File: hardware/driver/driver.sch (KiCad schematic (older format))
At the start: 32 parts, among them J1 Conn_01x02, J2 Conn_01x02, J3 Conn_01x04, J4 Conn_01x04, J6 Conn_01x02, Q1 IRF9Z34NPBF, Q2 IRF9Z34NPBF, Q3 IRFZ24NPBF, Q4 IRFZ24NPBF, U1 TC4420CPA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

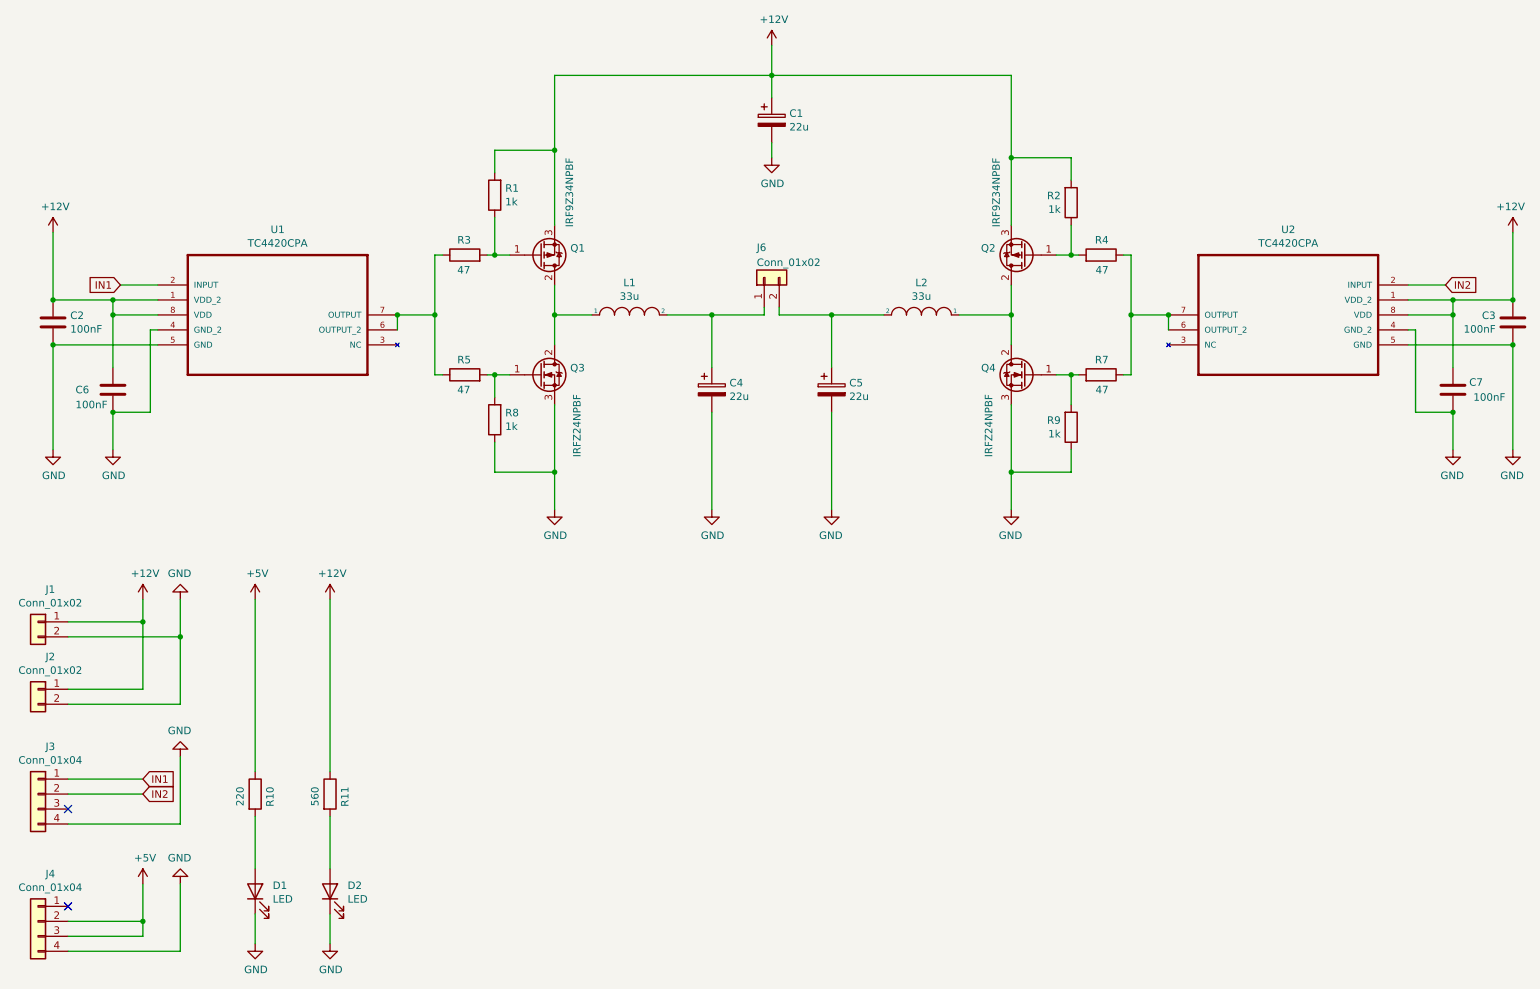
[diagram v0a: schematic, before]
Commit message: Update driver board
Driver board v0.1
Apart from removing temperature sensor connector, there are some minor changes:
- some tracks, such as 12V line near Q1 and Q3, were changed;
- 12V connectors are now moved to the "front panel" of the board.
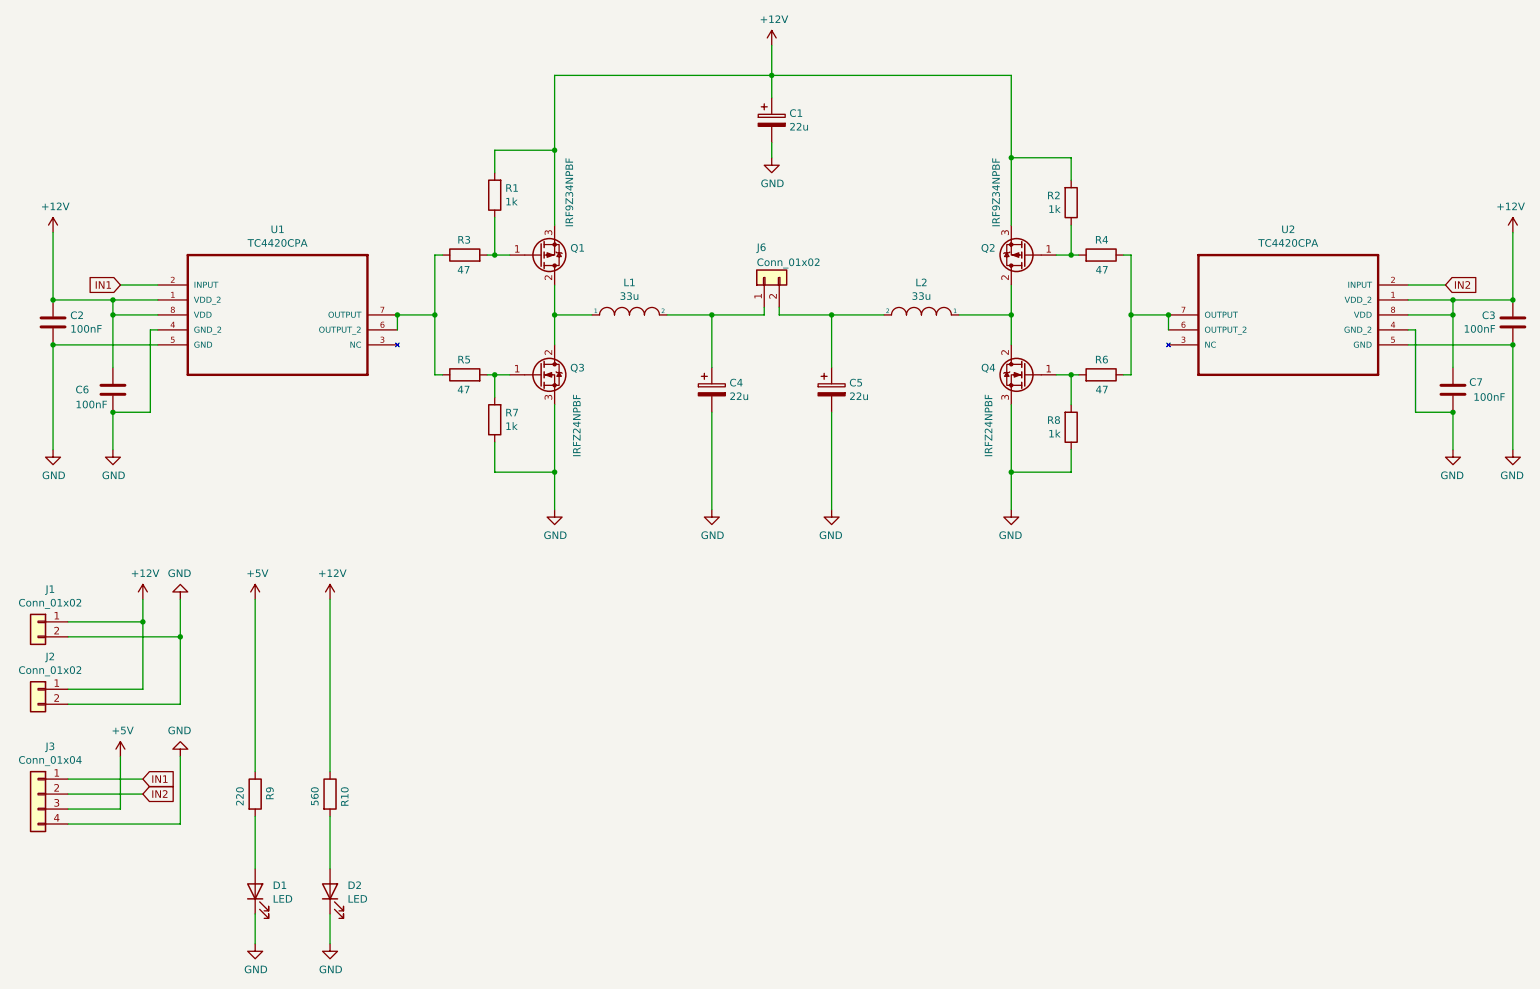
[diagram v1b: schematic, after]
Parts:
- removed J4: Conn_01x04, Connector_JST:JST_XH_B4B-XH-A_1x04_P2.50mm_Vertical, symbol Connector_Generic:Conn_01x04
- renumbered R11 to R10, R7 to R6, R8 to R7, R9 to R8, R10 to R9
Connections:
- net +5V: now also J3.3 (Pin_3)
- no-connect marks 2 -> 0
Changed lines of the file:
@@
 Wire Wire Line
 	950  6400 1450 6400
-$Comp
-L power:+5V #PWR08
-U 1 1 5F591312
-P 1450 7100
-F 0 "#PWR08" H 1450 6950 50  0001 C CNN
-F 1 "+5V" H 1465 7273 50  0000 C CNN
-F 2 "" H 1450 7100 50  0001 C CNN
-F 3 "" H 1450 7100 50  0001 C CNN
-	1    1450 7100
-	1    0    0    -1
-$EndComp
-$Comp
-L Connector_Generic:Conn_01x04 J4
-U 1 1 5F59DECB
-P 750 7350
-F 0 "J4" H 668 7667 50  0000 C CNN
-F 1 "Conn_01x04" H 668 7576 50  0000 C CNN
-F 2 "Connector_JST:JST_XH_B4B-XH-A_1x04_P2.50mm_Vertical" H 750 7350 50  0001 C CNN
-F 3 "~" H 750 7350 50  0001 C CNN
-	1    750  7350
-	-1   0    0    -1
-$EndComp
-$Comp
-L power:GND #PWR06
-U 1 1 5F59FAE5
-P 1700 7100
-F 0 "#PWR06" H 1700 6850 50  0001 C CNN
-F 1 "GND" H 1705 6927 50  0000 C CNN
-F 2 "" H 1700 7100 50  0001 C CNN
-F 3 "" H 1700 7100 50  0001 C CNN
-	1    1700 7100
-	-1   0    0    1
-$EndComp
 Text GLabel 1450 6500 2    50   Input ~ 0
 IN2
@@
 $EndComp
 $Comp
-L Device:R R8
+L Device:R R7
 U 1 1 5F64F957
 P 3800 4000
-F 0 "R8" H 3730 3954 50  0000 R CNN
+F 0 "R7" H 3730 3954 50  0000 R CNN
 F 1 "1k" H 3730 4045 50  0000 R CNN
 F 2 "Resistor_THT:R_Box_L13.0mm_W4.0mm_P9.00mm" V 3730 4000 50  0001 C CNN
@@
 Wire Wire Line
 	7650 2900 7550 2900
-$Comp
-L Device:R R9
-U 1 1 5F69B88C
-P 7650 4050
-F 0 "R9" H 7580 4004 50  0000 R CNN
-F 1 "1k" H 7580 4095 50  0000 R CNN
-F 2 "Resistor_THT:R_Box_L13.0mm_W4.0mm_P9.00mm" V 7580 4050 50  0001 C CNN
-F 3 "~" H 7650 4050 50  0001 C CNN
-	1    7650 4050
-	1    0    0    1
-$EndComp
 Wire Wire Line
 	7650 3900 7650 3700
@@
 	0    -1   -1   0
 $EndComp
-$Comp
-L Device:R R10
-U 1 1 5F6C1F80
-P 2200 6500
-F 0 "R10" V 2300 6550 50  0000 R CNN
-F 1 "220" V 2100 6550 50  0000 R CNN
-F 2 "Resistor_THT:R_Box_L13.0mm_W4.0mm_P9.00mm" V 2130 6500 50  0001 C CNN
-F 3 "~" H 2200 6500 50  0001 C CNN
-	1    2200 6500
-	1    0    0    -1
-$EndComp
 Wire Wire Line
 	2200 7000 2200 6650
@@
 $EndComp
 $Comp
-L Device:R R7
+L Device:R R6
 U 1 1 5F6331C6
 P 7850 3700
-F 0 "R7" V 7950 3750 50  0000 R CNN
+F 0 "R6" V 7950 3750 50  0000 R CNN
 F 1 "47" V 7750 3750 50  0000 R CNN
 F 2 "Resistor_THT:R_Box_L13.0mm_W4.0mm_P9.00mm" V 7780 3700 50  0001 C CNN
@@
 	0    -1   -1   0
 $EndComp
-$Comp
-L Device:R R11
-U 1 1 5F6D669A
-P 2700 6500
-F 0 "R11" V 2800 6550 50  0000 R CNN
-F 1 "560" V 2600 6550 50  0000 R CNN
-F 2 "Resistor_THT:R_Box_L13.0mm_W4.0mm_P9.00mm" V 2630 6500 50  0001 C CNN
-F 3 "~" H 2700 6500 50  0001 C CNN
-	1    2700 6500
-	1    0    0    -1
-$EndComp
 Wire Wire Line
 	2700 7000 2700 6650
@@
 Wire Wire Line
 	1700 6250 1700 6700
-NoConn ~ 950  6600
-Wire Wire Line
-	950  7450 1450 7450
-Wire Wire Line
-	1450 7100 1450 7350
-Wire Wire Line
-	1700 7100 1700 7550
-Wire Wire Line
-	950  7550 1700 7550
 Wire Wire Line
 	1700 5450 1700 5900
@@
 	-1   0    0    1
 $EndComp
-NoConn ~ 950  7250
-Wire Wire Line
-	950  7350 1450 7350
-Connection ~ 1450 7350
-Wire Wire Line
-	1450 7350 1450 7450
+$Comp
+L Device:R R10
+U 1 1 5F6D669A
+P 2700 6500
+F 0 "R10" V 2800 6550 50  0000 R CNN
+F 1 "560" V 2600 6550 50  0000 R CNN
+F 2 "Resistor_THT:R_Box_L13.0mm_W4.0mm_P9.00mm" V 2630 6500 50  0001 C CNN
+F 3 "~" H 2700 6500 50  0001 C CNN
+	1    2700 6500
+	1    0    0    -1
+$EndComp
+$Comp
+L Device:R R9
+U 1 1 5F6C1F80
+P 2200 6500
+F 0 "R9" V 2300 6550 50  0000 R CNN
+F 1 "220" V 2100 6550 50  0000 R CNN
+F 2 "Resistor_THT:R_Box_L13.0mm_W4.0mm_P9.00mm" V 2130 6500 50  0001 C CNN
+F 3 "~" H 2200 6500 50  0001 C CNN
+	1    2200 6500
+	1    0    0    -1
+$EndComp
+$Comp
+L Device:R R8
+U 1 1 5F69B88C
+P 7650 4050
+F 0 "R8" H 7580 4004 50  0000 R CNN
+F 1 "1k" H 7580 4095 50  0000 R CNN
+F 2 "Resistor_THT:R_Box_L13.0mm_W4.0mm_P9.00mm" V 7580 4050 50  0001 C CNN
+F 3 "~" H 7650 4050 50  0001 C CNN
+	1    7650 4050
+	1    0    0    1
+$EndComp
+$Comp
+L power:+5V #PWR?
+U 1 1 60A6900B
+P 1300 6250
+F 0 "#PWR?" H 1300 6100 50  0001 C CNN
+F 1 "+5V" H 1315 6423 50  0000 C CNN
+F 2 "" H 1300 6250 50  0001 C CNN
+F 3 "" H 1300 6250 50  0001 C CNN
+	1    1300 6250
+	1    0    0    -1
+$EndComp
+Wire Wire Line
+	950  6600 1300 6600
+Wire Wire Line
+	1300 6600 1300 6250
 $EndSCHEMATC
